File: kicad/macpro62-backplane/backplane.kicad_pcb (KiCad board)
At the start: 6 copper layers, 122 x 122 mm, 30 parts, among them J1 CPU-LINK: Amphenol Mini Cool 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, J10 MCIO 124 OUT -> Face S (x4 wi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, J2 PSU-IN: Micro-Fit 3.0 2x4 (12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, J3 FACE-P AUX: JST GH 14P (PWR_E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, J4 FACE-S AUX: JST GH 14P (same 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, J5 FAN: GH 4P (12V, GND, PWM, FG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, J6 IOB-LINK: GH 15P (PWRBTN, HAL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, J7 OpenCore boot: M.2 M-key sock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, J8 SWD (3V3, SWCLK, SWDIO, GND), J9 MCIO 124 OUT -> Face P (x16, 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, SW1 BOOTSEL, SW2 Bench power button, U1 RP2350A (LCSC C42411118), U10 OPTION Gen5: DS320PR810 #1, F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, U11 OPTION Gen5: DS320PR810 #2, F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, U12 OPTION Gen5: DS320PR810 #3, F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, U13 OPTION Gen5: DS320PR810 #4, F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, U14 OPTION Gen5: DS320PR810 #5, F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, U2 W25Q128 QSPI flash (part TBD), U3 TMP1075 core-base temp sensor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, U4 TMP1075 core-base temp sensor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, Y1 12 MHz crystal

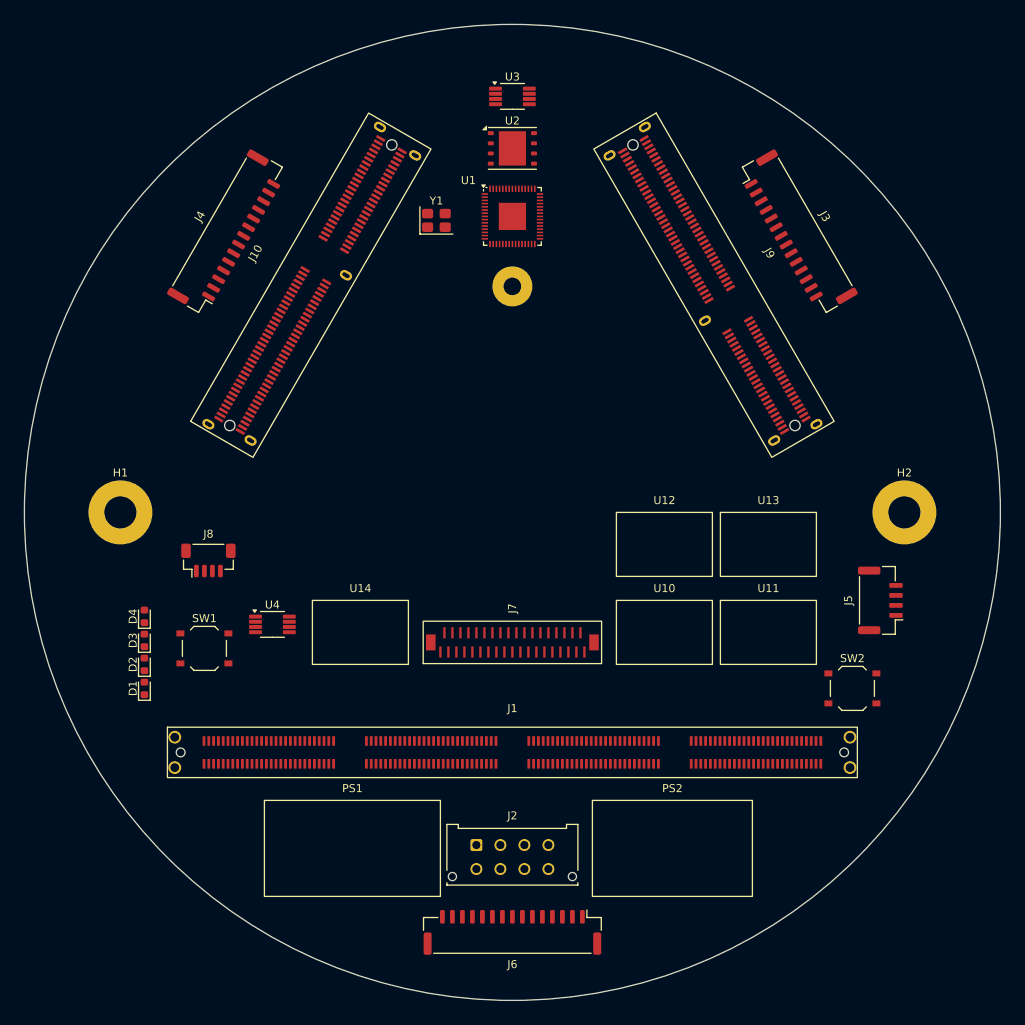
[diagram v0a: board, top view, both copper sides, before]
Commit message: Cross-board compatibility audit: interface control doc, CR-BP-1 applied, J2/J3 row-swap pinouts, 15-pin face AUX, fan header removed from backplane, CPU board i226/BT1 cleanup
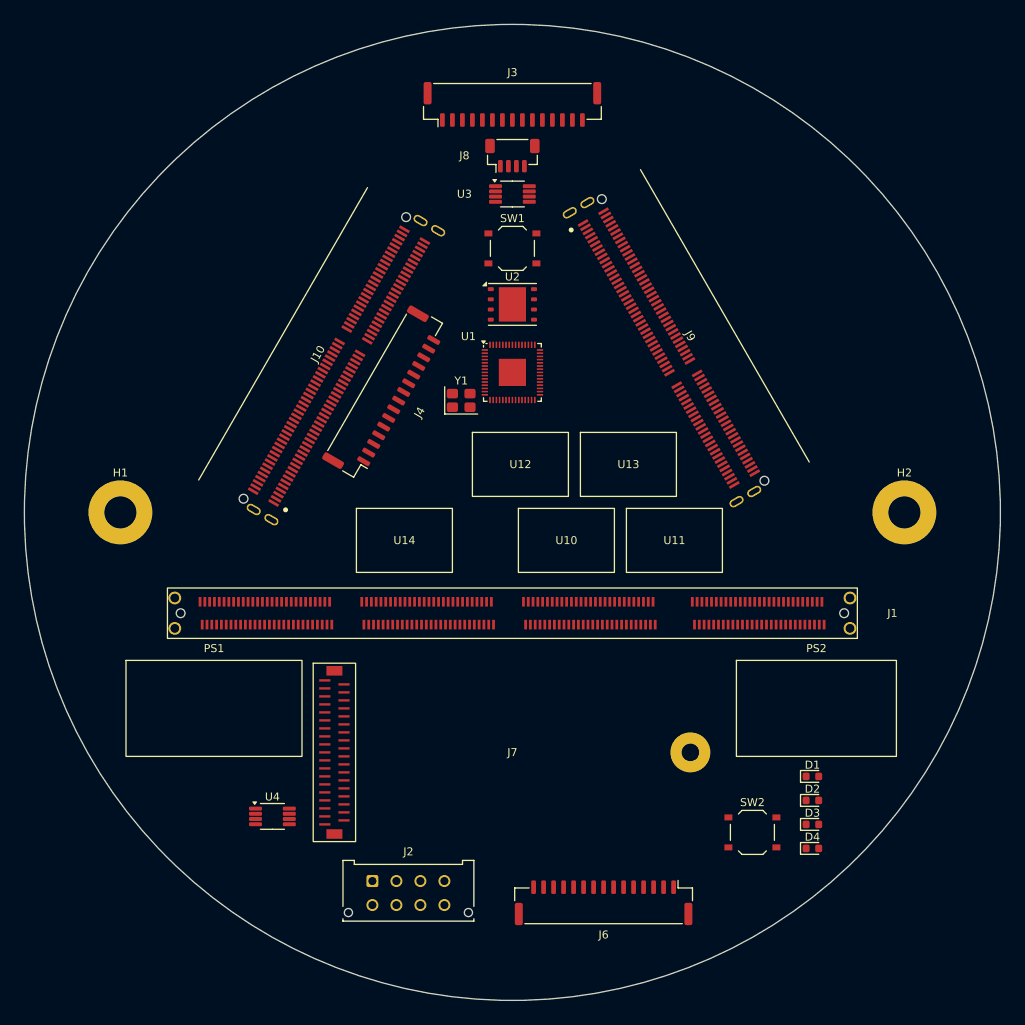
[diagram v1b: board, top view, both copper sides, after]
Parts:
- removed J5: FAN: GH 4P (12V, GND, PWM, FG) - harness to top interposer,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, Connector_JST:JST_GH_BM04B-GHS-TBT_1x04-1MP_P1.25mm_Vertical
- J1: value CPU-LINK: Amphenol Mini Cool Edge 224P vertical (ME1022410103011) - CPU board card edge, MP62 hub pinout -> CPU-LINK: Amphenol Mini Cool Edge 224P vertical (ME1022410103011) at stock riser-slot position (ESTIMATE y=-12.6)
- J10: value MCIO 124 OUT -> Face S (x4 wired, REFCLK, PERST#, sideband) -> MCIO 124 RA OUT -> Face S (x4 wired, REFCLK, PERST#, sideband); cable exits radially under the Face S board edge; footprint MP62_Placeholders:MP62_MCIO_124P_Vertical_SMT_TE2360189_PLACEHOLDER -> MP62_Placeholders:MP62_MCIO_124P_RA_SFF-TA-1016
- J3: value FACE-P AUX: JST GH 14P (PWR_EN, PWR_GOOD, SMBus, THERM, PRSNT, 3V3_AUX, USB2 fallback) -> FACE-P AUX: JST GH 15P (MP62-FACE v0.1 J_AUX: PWR_EN, PWR_GOOD, SMBus, THERM, PRSNT, 3V3_AUX, USB2, MOD_LED#); footprint Connector_JST:JST_GH_BM14B-GHS-TBT_1x14-1MP_P1.25mm_Vertical -> Connector_JST:JST_GH_BM15B-GHS-TBT_1x15-1MP_P1.25mm_Vertical
- J4: value FACE-S AUX: JST GH 14P (same pinout as J3) -> FACE-S AUX: JST GH 15P (same pinout as J3); footprint Connector_JST:JST_GH_BM14B-GHS-TBT_1x14-1MP_P1.25mm_Vertical -> Connector_JST:JST_GH_BM15B-GHS-TBT_1x15-1MP_P1.25mm_Vertical
- J6: value IOB-LINK: GH 15P (PWRBTN, HALL x2, LED I2C, USB2, 3V3_SB, GND) -> IOB-LINK: GH 15P <-> IOB J6 (3V3_SB x2, PWRBTN_IN_N, HALL_A/B_N, I2C_SYS, IOB_INT_N, IOB_PRSNT_N, USB2_LINK, GND)
- J7: value OpenCore boot: M.2 M-key socket, SATA0, 2242 card (card toward +y; PCIe may route under the card on L1/L6) -> OpenCore boot: M.2 M-key socket, SATA0, 2242 card (PSU side; height under PSU TBD M7)
- J9: value MCIO 124 OUT -> Face P (x16, REFCLK, PERST#, sideband) -> MCIO 124 RA OUT -> Face P (x16, REFCLK, PERST#, sideband); cable exits radially under the Face P board edge; footprint MP62_Placeholders:MP62_MCIO_124P_Vertical_SMT_TE2360189_PLACEHOLDER -> MP62_Placeholders:MP62_MCIO_124P_RA_SFF-TA-1016
- U3: value TMP1075 core-base temp sensor #1 -> TMP1075 core-base temp sensor #1 (under core bottom, I2C_SYS 0x48)
- U4: value TMP1075 core-base temp sensor #2 -> TMP1075 PSU-side temp sensor #2 (I2C_SYS 0x49)
- moved D4 88.4 mm to (187.5, 142.0), turned to 0 degrees
- moved D3 86.6 mm to (187.5, 139.0), turned to 0 degrees
- moved D2 85.2 mm to (187.5, 136.0), turned to 0 degrees
- moved D1 84.2 mm to (187.5, 133.0), turned to 0 degrees
- moved J8 63.3 mm to (150.0, 55.4)
- moved SW1 63.1 mm to (150.0, 67.0)
- moved J3 39.0 mm to (150.0, 49.0), turned to 0 degrees
- moved J4 28.1 mm to (134.1, 85.1)
- moved J7 26.2 mm to (127.8, 130.0), turned to 0 degrees
- moved PS2 25.1 mm to (188.0, 124.5)
- moved PS1 24.6 mm to (112.7, 124.5)
- moved U4 24.0 mm to (120.0, 138.0)
- moved Y1 22.7 mm to (143.6, 86.0)
- moved SW2 21.9 mm to (180.0, 140.0)
- moved U12 20.6 mm to (151.0, 94.0)
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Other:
- board text added: "CPU board plane (ESTIMATED from stock slot photo, d~12.6, TBD)"
- board text added: "CPU carrier 224 card (79.89 x 1.57) enters J1 here (J1 at 180 deg: A row = host TX on the PSU side, A1 at +x); parts within ~6 mm: height <= shoulder gap (M3)"
- board text added: "Face P board plane MEASURED ~55 mm (M2), bottom edge ~15 mm above BP (M1)"
- board text added: "Face S board plane MEASURED ~55 mm (M2), bottom edge ~15 mm above BP (M1)"
- board text added: "J_PCIE (module X 43.5, s=+8.5); BP receptacle s=+8.0 -> cable jog 0.5 mm"
- board text added: "J_PCIE (module X 43.5, s=+8.5); BP receptacle s=-5.0 -> cable jog 13.5 mm"
- board text added: "MCIO cable exit zone: plug ~9-10 mm high passes under the 15 mm board edge, bends up outside"
- board text added: "PSU SIDE (behind CPU board, under PSU): heights TBD (M7)"
- board text added: "S1 stock hole: D6 keep-out (CR-BP-1)"
- board text added: "S2 stock hole: D6 keep-out (CR-BP-1)"
- board text added: "S3 stock hole: D6 keep-out (CR-BP-1)"
- board text added: "S4 stock hole: D6 keep-out (CR-BP-1)"
- board text added: "S5 stock hole: D6 keep-out (CR-BP-1)"
- board text added: "S6 stock hole: D6 keep-out (CR-BP-1)"
- board text added: "open core interior / air path above the region bounded by the 3 board planes (plane-triangle incentre (0, 28.3), inradius ~41; disc centre is under the core, 12.6 mm inside the CPU board)"
- board text removed: "CPU board (1.57 mm card edge, shoulder 105 mm) enters J1 here; parts within ~6 mm of this line: height <= shoulder gap (M3)"
- board text removed: "CPU face bottom-edge chord ASSUMED d=30 mm (TBD)"
- board text removed: "Face P (primary) bottom-edge chord ASSUMED d=30 mm (TBD)"
- board text removed: "Face S (secondary) bottom-edge chord ASSUMED d=30 mm (TBD)"
- board text removed: "Optional cutout zone (not cut): core-channel air/cable relief - only if M1 shows airflow from below"

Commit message: ICD rev 2: 45 deg faces, 445 W ceiling + live power target (INA228 telemetry), ribbon MCIO jog cables, BT on S0, fan fail-safe, port-module I2C map
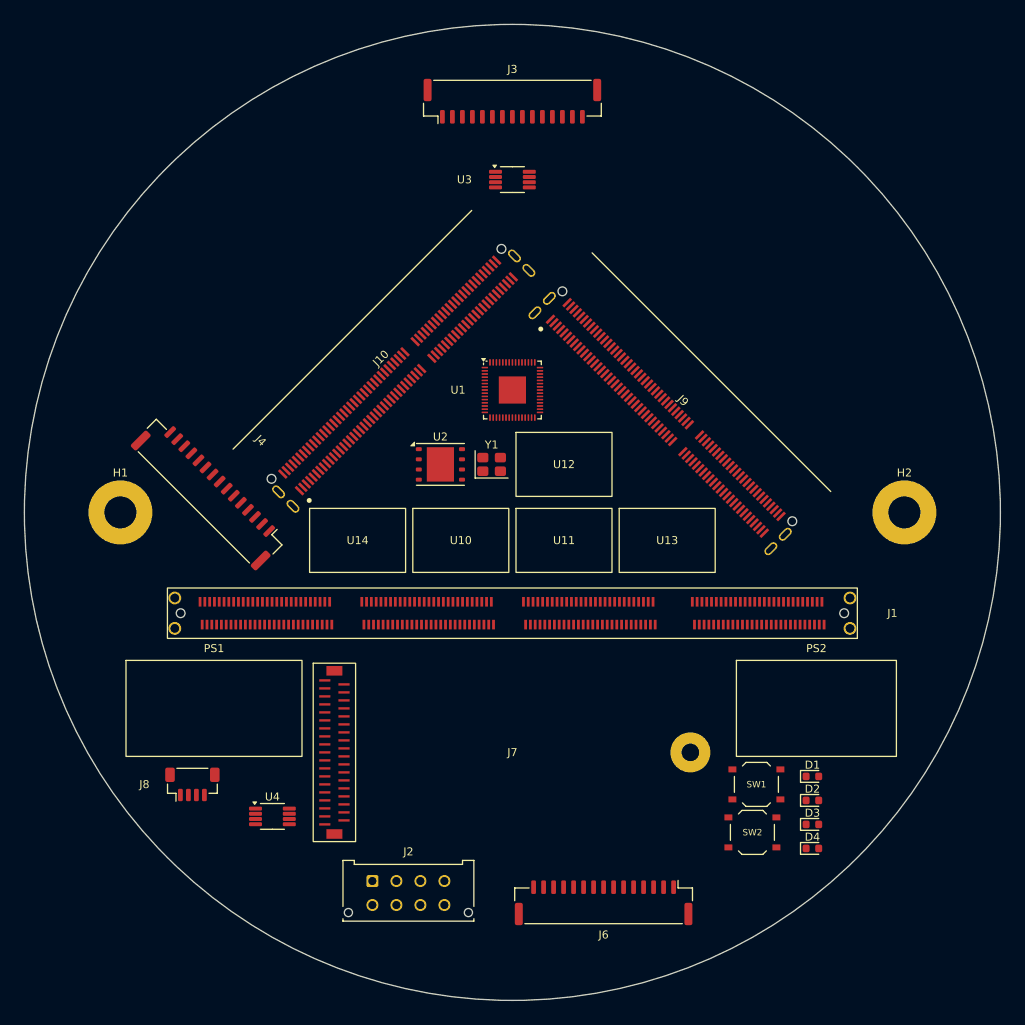
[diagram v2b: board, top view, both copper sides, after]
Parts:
- J8: value SWD (3V3, SWCLK, SWDIO, GND) -> SWD (3V3, SWCLK, SWDIO, GND) (fp5: PSU side)
- SW1: value BOOTSEL -> BOOTSEL (fp5: PSU side)
- moved J8 88.2 mm to (110.0, 134.0)
- moved SW1 73.6 mm to (180.5, 134.0)
- moved J4 25.4 mm to (112.0, 97.5), turned to 135 degrees
- moved U2 21.9 mm to (141.0, 94.0)
- moved U11 13.8 mm to (156.4, 103.5)
- moved U10 13.2 mm to (143.6, 103.5)
- moved U13 10.7 mm to (169.3, 103.5)
- moved Y1 8.86 mm to (147.4, 94.0)
- moved J9 8.32 mm to (170.6, 86.7), turned to -45 degrees
- moved J10 7.74 mm to (134.3, 81.4), turned to 45 degrees
- moved U14 5.85 mm to (130.7, 103.5)
- moved U12 5.45 mm to (156.4, 94.0)
- moved U1 2.20 mm to (150.0, 84.7)
- moved U3 1.80 mm to (150.0, 58.4)
- moved J3 0.40 mm to (150.0, 48.6)
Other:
- board text added: "CPU board plane (slot measured -12.5 +/- 0.3 on the scan, M2b)"
- board text added: "Face P board plane ~55 mm (M2) at 45 deg (M2c, Aidan ~45), bottom edge ~15 mm above BP (M1)"
- board text added: "Face S board plane ~55 mm (M2) at 135 deg (M2c, Aidan ~45), bottom edge ~15 mm above BP (M1)"
- board text added: "J_PCIE (module X 43.5, s=+8.5); BP receptacle s=-2.0 -> cable jog 10.5 mm"
- board text added: "J_PCIE (module X 43.5, s=+8.5); BP receptacle s=-5.2 -> cable jog 13.7 mm"
- board text added: "MCIO exit: plug 8.2 high under the 15 mm board edge; flat twinax bends up outside (R >= 3 per layer), jog 10.5 mm"
- board text added: "MCIO exit: plug 8.2 high under the 15 mm board edge; flat twinax bends up outside (R >= 3 per layer), jog 13.7 mm"
- board text added: "open core interior / air path above the region bounded by the 3 board planes (45/135 deg: incentre (0, 24.8), inradius ~37; disc centre 12.6 mm inside the CPU board)"
- board text removed: "CPU board plane (ESTIMATED from stock slot photo, d~12.6, TBD)"
- board text removed: "Face P board plane MEASURED ~55 mm (M2), bottom edge ~15 mm above BP (M1)"
- board text removed: "Face S board plane MEASURED ~55 mm (M2), bottom edge ~15 mm above BP (M1)"
- board text removed: "J_PCIE (module X 43.5, s=+8.5); BP receptacle s=+8.0 -> cable jog 0.5 mm"
- board text removed: "J_PCIE (module X 43.5, s=+8.5); BP receptacle s=-5.0 -> cable jog 13.5 mm"
- board text removed: "MCIO cable exit zone: plug ~9-10 mm high passes under the 15 mm board edge, bends up outside"
- board text removed: "open core interior / air path above the region bounded by the 3 board planes (plane-triangle incentre (0, 28.3), inradius ~41; disc centre is under the core, 12.6 mm inside the CPU board)"

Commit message: O-10: zero-jog MCIO (face J_PCIE X47.0, J_DISP X82.5, narrow plugs), backplane fp6 re-pack, ICD rev 3
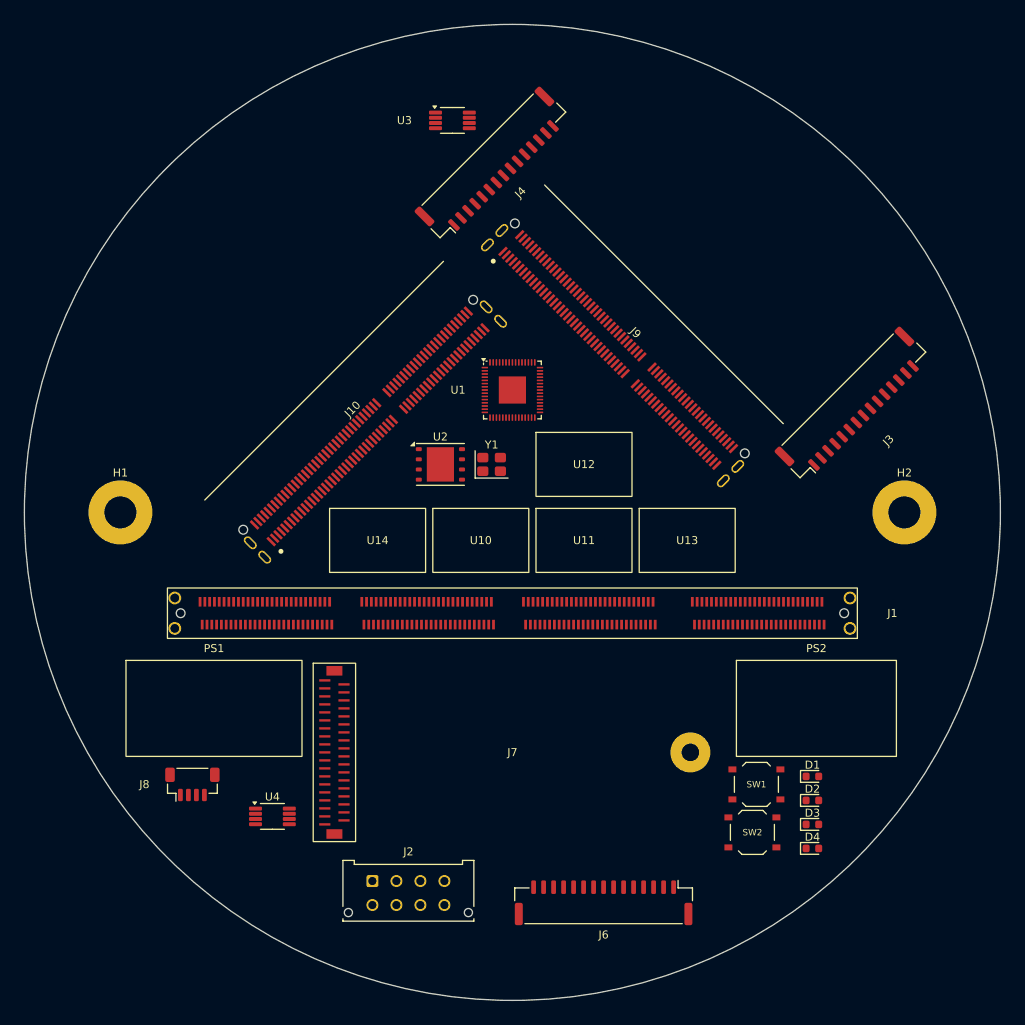
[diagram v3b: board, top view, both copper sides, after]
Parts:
- moved J3 56.9 mm to (192.5, 86.5), turned to 45 degrees
- moved J4 54.2 mm to (147.5, 56.5), turned to 45 degrees
- moved U3 10.5 mm to (142.5, 51.0)
- moved J9 10.4 mm to (164.7, 78.2)
- moved J10 7.28 mm to (130.7, 87.8)
- moved U10 2.50 mm to (146.1, 103.5)
- moved U11 2.50 mm to (158.9, 103.5)
- moved U12 2.50 mm to (158.9, 94.0)
- moved U13 2.50 mm to (171.8, 103.5)
- moved U14 2.50 mm to (133.2, 103.5)
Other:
- board text added: "J_PCIE (module X 47.0, s=+5.0); BP receptacle s=+5.0 -> cable jog 0.0 mm (zero, O-10)"
- board text added: "MCIO ribbon corridor (no parts): narrow straight plug (<= 10.0 high) ends n 41.5; ribbon ~10 mm under the 15 mm board edge, bends up outside (R >= 3), jog 0.0"
- board text added: "MCIO ribbon corridor (no parts): narrow straight plug (<= 10.0 high) ends n 45.0; ribbon ~10 mm under the 15 mm board edge, bends up outside (R >= 3), jog 0.0"
- board text added: "fp6 (ICD O-10): J9/J10 land at s = +5.0 = module J_PCIE X 47.0 (zero jog); straight-straight MCIO 124 cable, NARROW plugs."
- board text removed: "J_PCIE (module X 43.5, s=+8.5); BP receptacle s=-2.0 -> cable jog 10.5 mm"
- board text removed: "J_PCIE (module X 43.5, s=+8.5); BP receptacle s=-5.2 -> cable jog 13.7 mm"
- board text removed: "MCIO exit: plug 8.2 high under the 15 mm board edge; flat twinax bends up outside (R >= 3 per layer), jog 10.5 mm"
- board text removed: "MCIO exit: plug 8.2 high under the 15 mm board edge; flat twinax bends up outside (R >= 3 per layer), jog 13.7 mm"
